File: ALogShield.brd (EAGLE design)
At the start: 53.3 x 78.5 mm, 29 parts, among them U1 DS3231MZ/V+T

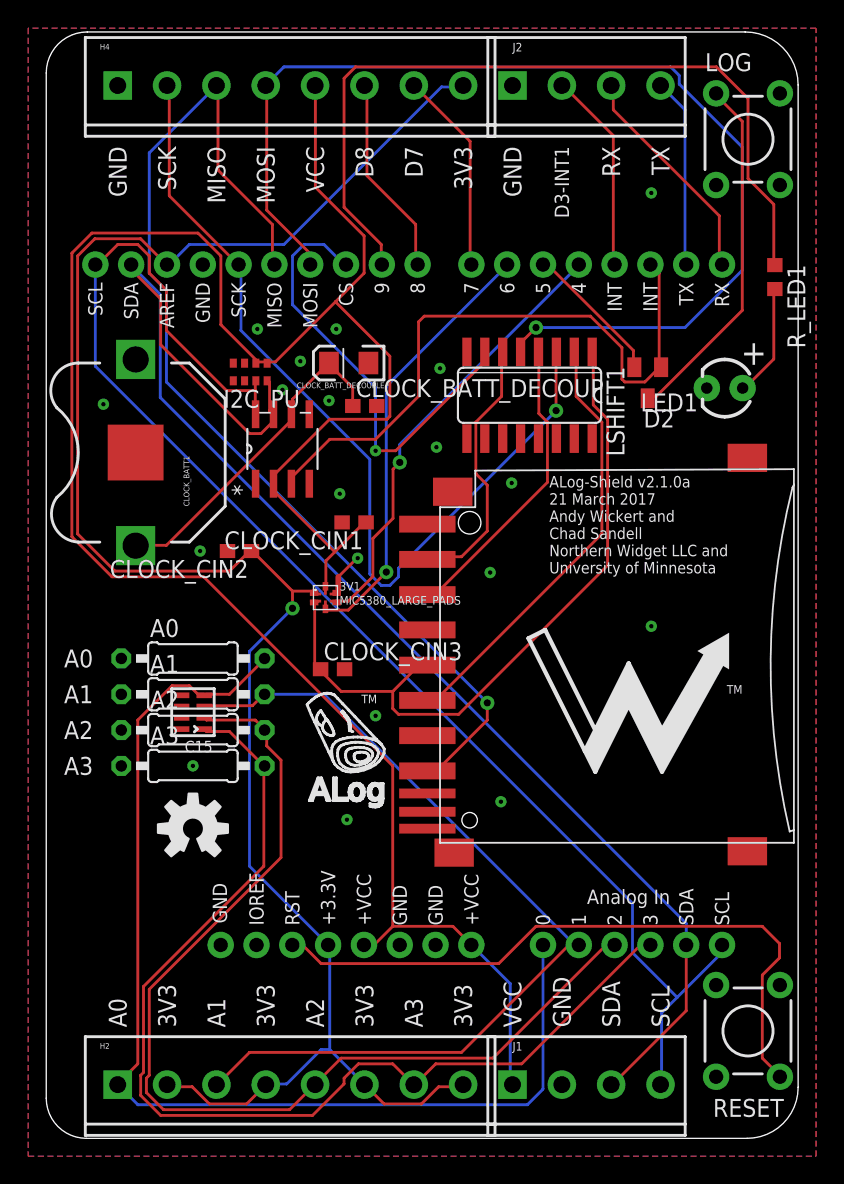
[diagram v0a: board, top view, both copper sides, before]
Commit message: SMD battery clip
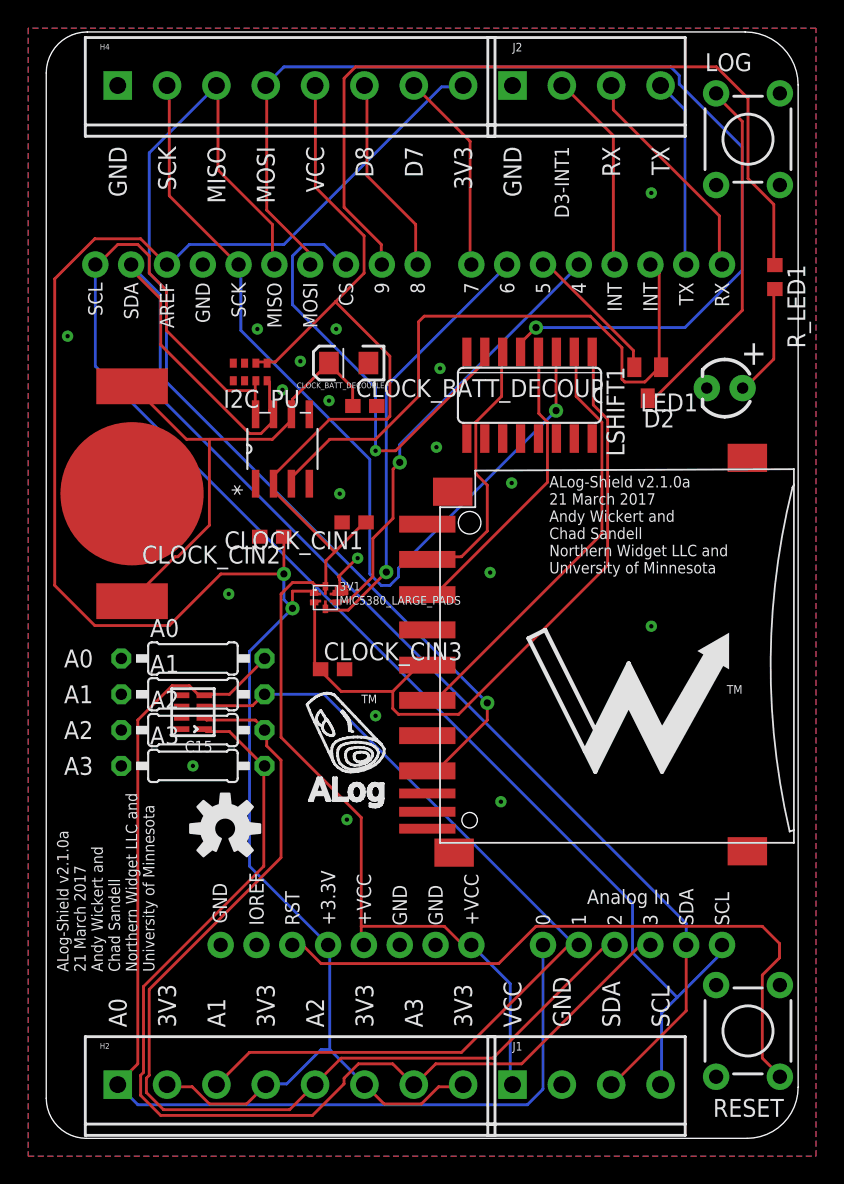
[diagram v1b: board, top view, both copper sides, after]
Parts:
- removed CLOCK_BATT1: 3V Backup Battery, SparkFun:BATTCON_12MM_PTH
- added CLOCK_BATT: Linx BAT-HLD-012-SMT, awickert:LINX_BAT-HLD-012-SMT
- moved CLOCK_CIN2 2.50 mm to (16.0, 42.7)
- moved LOGO2 2.29 mm to (12.7, 22.0)
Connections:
- net BAT: now also CLOCK_BATT.POWER0, CLOCK_BATT.POWER1; no longer CLOCK_BATT1.VCC@1
- net GND: now also CLOCK_BATT.GND; no longer CLOCK_BATT1.GND
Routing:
- net VCC: track 159.4 -> 108.5 mm
- net BAT: track 23.6 -> 36.3 mm
- net +3V3: track 134.9 -> 145.4 mm, vias 1 -> 2
- net GND: track 3.52 -> 8.51 mm

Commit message: Remove 3V3; connect 3V3 and VDD
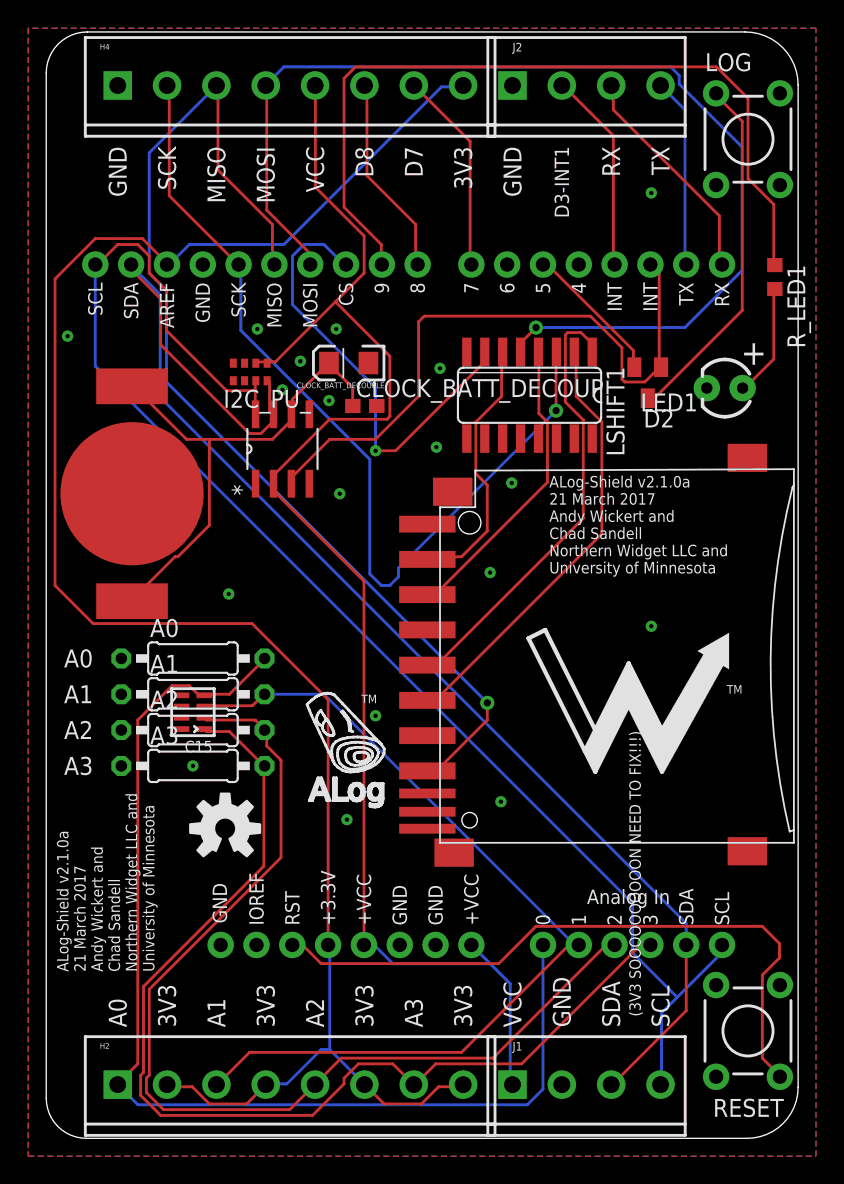
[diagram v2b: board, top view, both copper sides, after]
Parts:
- removed 3V1: MIC5380_LARGE_PADS, csandell:6-TMLF_SMD_PADS
- removed CLOCK_CIN1, CLOCK_CIN2, CLOCK_CIN3: 1uF, rcl:C0603
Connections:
- net +3V3: no longer 3V1.1, 3V1.7, CLOCK_CIN2.1
- net D4-SENSE_LDO_SWITCH: no longer 3V1.10, 3V1.4
- net D6-CLOCK_SD_SWITCH: no longer 3V1.3, 3V1.9
- net GND: no longer 3V1.11, 3V1.5, CLOCK_CIN1.2, CLOCK_CIN2.2, CLOCK_CIN3.2
- net VCC: no longer 3V1.12, 3V1.6, CLOCK_CIN1.1
- net VDD: no longer 3V1.2, 3V1.8, CLOCK_CIN3.1
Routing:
- net D4-SENSE_LDO_SWITCH: track 31.7 -> 0.00 mm, vias 1 -> 0
- net D6-CLOCK_SD_SWITCH: track 31.0 -> 0.00 mm, vias 1 -> 0
- net VDD: track 50.7 -> 31.8 mm
- net +3V3: track 145.4 -> 130.9 mm, vias 2 -> 0
- net GND: track 8.51 -> 0.29 mm, vias 19 -> 18
- net VCC: track 108.5 -> 101.5 mm
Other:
- board text added: "(3V3 SOOOOOOOOOON NEED TO FIX!!!)"

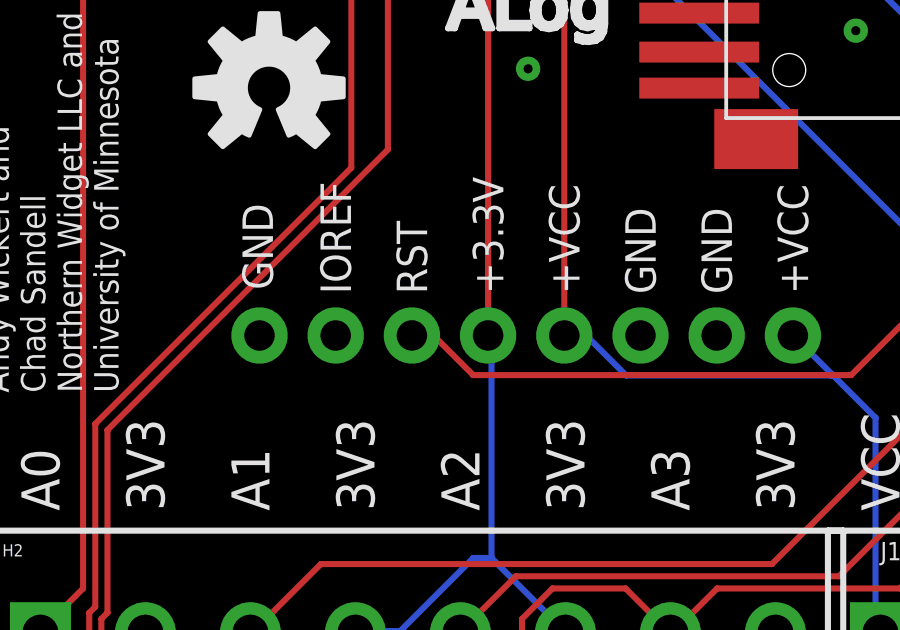
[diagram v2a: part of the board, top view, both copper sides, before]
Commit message: IOREF to VCC
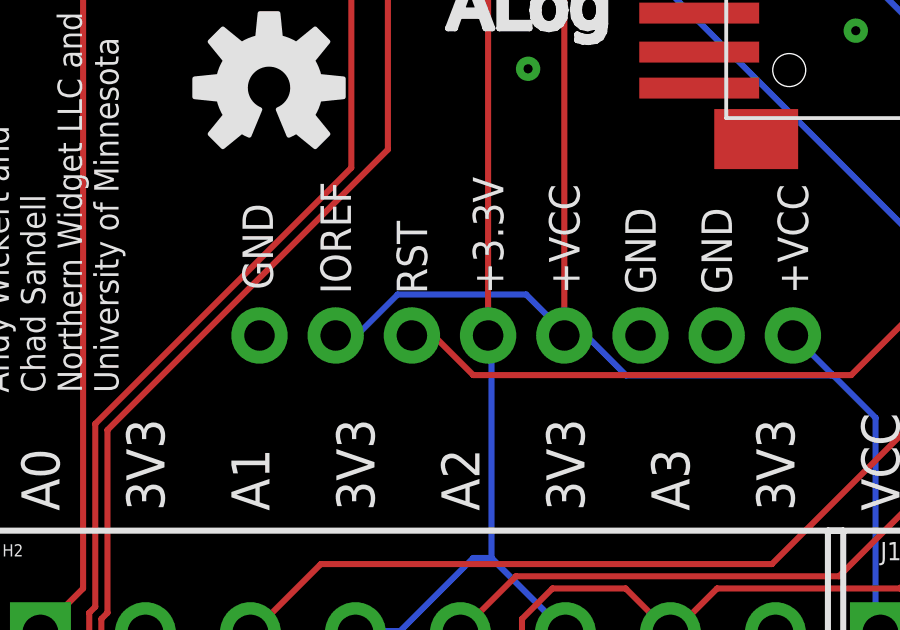
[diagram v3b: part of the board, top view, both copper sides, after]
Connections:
- net GND: no longer U$9.IOREF
- net VCC: now also U$9.IOREF
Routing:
- net VCC: track 101.5 -> 110.4 mm
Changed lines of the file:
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@@
 <contactref element="U$9" pad="GND@2"/>
 <contactref element="U$9" pad="NC"/>
-<contactref element="U$9" pad="IOREF"/>
 <contactref element="U1" pad="5"/>
 <contactref element="LSHIFT1" pad="8"/>
@@
 <wire x1="16.1925" y1="46.355" x2="16.1925" y2="45.87875" width="0.2032" layer="1"/>
 <wire x1="16.1925" y1="46.355" x2="16.129" y2="46.4312" width="0.2032" layer="1"/>
+<contactref element="U$9" pad="IOREF"/>
+<wire x1="15.71625" y1="13.81125" x2="14.9225" y2="13.81125" width="0.2032" layer="16"/>
+<wire x1="16.98625" y1="15.08125" x2="15.71625" y2="13.81125" width="0.2032" layer="16"/>
+<wire x1="21.2725" y1="15.08125" x2="16.98625" y2="15.08125" width="0.2032" layer="16"/>
+<wire x1="22.5425" y1="13.81125" x2="21.2725" y2="15.08125" width="0.2032" layer="16"/>
+<wire x1="14.9225" y1="13.81125" x2="14.9225" y2="13.716" width="0.2032" layer="16"/>
+<wire x1="22.5425" y1="13.81125" x2="22.5425" y2="13.716" width="0.2032" layer="16"/>
 </signal>
 <signal name="DI">
